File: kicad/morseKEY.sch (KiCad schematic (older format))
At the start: 11 parts

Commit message: schematic
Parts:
- removed P?: CONN_01X02, symbol CONN_01X02
- added P2: KEY, Pin_Headers:Pin_Header_Straight_1x03, symbol CONN_01X03
- added P3: ISP, Pin_Headers:Pin_Header_Straight_2x03, symbol CONN_02X03
- added R4: 2k2, Pin_Headers:Pin_Header_Straight_1x03, symbol R_VAR
- added R5: 2k2, Resistors_ThroughHole:Resistor_Horizontal_RM10mm, symbol R
- C1: renamed from C?; value C -> 100nF; footprint (none) -> Capacitors_ThroughHole:C_Disc_D3_P2.5
- C2: renamed from C?; value C -> 33uF,10V; footprint (none) -> Capacitors_ThroughHole:C_Radial_D5_L6_P2.5; symbol C -> C_POL; manf# (none) -> mfr_pn
- D1, D2: renamed from D?; value ZENERsmall -> 3V6; footprint (none) -> Diodes_ThroughHole:Diode_DO-35_SOD27_Horizontal_RM10
- P1: renamed from P?; footprint (none) -> Connect:USB_A
- R1: renamed from R?; value R -> 2k2; footprint (none) -> Resistors_ThroughHole:Resistor_Horizontal_RM10mm
- R2, R3: renamed from R?; value R -> 68E; footprint (none) -> Resistors_ThroughHole:Resistor_Horizontal_RM10mm
- SP1: renamed from SP?; value SPEAKER -> BUZ; footprint (none) -> Pin_Headers:Pin_Header_Straight_1x02
- U1: renamed from IC?; footprint DIP8 -> Housings_DIP:DIP-8_W7.62mm_LongPads
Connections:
- net labels added: 5V, D+, D-, GND, K1, K3, MISO, MOSI, RST, SCK
- wire segments 0 -> 59
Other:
- moved on the sheet: C1, C2, D1, D2, P1, R1, R2, R3

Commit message: board layout
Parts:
- C1: footprint Capacitors_ThroughHole:C_Disc_D3_P2.5 -> morseKEY:C_Disc_D3_P2.5
- C2: footprint Capacitors_ThroughHole:C_Radial_D5_L6_P2.5 -> morseKEY:C_Radial_D5_L6_P2.5
- D1, D2: footprint Diodes_ThroughHole:Diode_DO-35_SOD27_Horizontal_RM10 -> morseKEY:Diode_DO-41_SOD81_Vertical_KathodeUp
- P1: footprint Connect:USB_A -> morseKEY:USB_A
- P2: footprint Pin_Headers:Pin_Header_Straight_1x03 -> morseKEY:Pin_Header_Straight_1x03
- P3: footprint Pin_Headers:Pin_Header_Straight_2x03 -> morseKEY:Pin_Header_Straight_2x03
- R1, R2, R3: footprint Resistors_ThroughHole:Resistor_Horizontal_RM10mm -> morseKEY:Resistor_Vertical_RM5mm
- R4: value 2k2 -> 2k5; footprint Pin_Headers:Pin_Header_Straight_1x03 -> morseKEY:Pin_Header_Straight_1x03
- R5: value 2k2 -> 2k5; footprint Resistors_ThroughHole:Resistor_Horizontal_RM10mm -> morseKEY:Resistor_Vertical_RM5mm
- SP1: footprint Pin_Headers:Pin_Header_Straight_1x02 -> morseKEY:Pin_Header_Straight_1x04; symbol SPEAKER -> SPEAKER2; manf# (none) -> Value
- U1: footprint Housings_DIP:DIP-8_W7.62mm_LongPads -> morseKEY:DIP-8_W7.62mm_LongPads
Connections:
- wire segments 59 -> 62
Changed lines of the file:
@@
 F 0 "U1" H 4575 4200 50  0000 C CNB
 F 1 "ATTINY85-P" H 4750 4125 50  0000 C CNB
-F 2 "Housings_DIP:DIP-8_W7.62mm_LongPads" H 6725 3725 50  0000 C CIN
+F 2 "morseKEY:DIP-8_W7.62mm_LongPads" H 6725 3725 50  0001 C CIN
 F 3 "" H 5725 3725 50  0000 C CNN
 	1    5725 3725
@@
 F 0 "C1" H 7400 2975 50  0000 L CNB
 F 1 "100nF" H 7400 2775 50  0000 L CNN
-F 2 "Capacitors_ThroughHole:C_Disc_D3_P2.5" H 7413 2725 50  0001 C CNN
+F 2 "morseKEY:C_Disc_D3_P2.5" H 7413 2725 50  0001 C CNN
 F 3 "" H 7375 2875 50  0000 C CNN
 	1    7375 2875
@@
 F 0 "C2" H 7775 2975 50  0000 L CNB
 F 1 "33uF,10V" H 7775 2775 50  0000 L CNN
-F 2 "Capacitors_ThroughHole:C_Radial_D5_L6_P2.5" H 7788 2725 50  0001 C CNN
+F 2 "morseKEY:C_Radial_D5_L6_P2.5" H 7788 2725 50  0001 C CNN
 F 3 "" H 7750 2875 50  0000 C CNN
 F 4 "mfr_pn" H 7750 2875 60  0001 C CNN "manf#"
@@
 F 0 "R2" V 8150 3575 50  0000 C CNB
 F 1 "68E" V 8250 3575 50  0000 C CNN
-F 2 "Resistors_ThroughHole:Resistor_Horizontal_RM10mm" V 8180 3575 50  0001 C CNN
+F 2 "morseKEY:Resistor_Vertical_RM5mm" V 8180 3575 50  0001 C CNN
 F 3 "" H 8250 3575 50  0000 C CNN
 	1    8250 3575
@@
 F 0 "R3" V 8350 3675 50  0000 C CNB
 F 1 "68E" V 8250 3675 50  0000 C CNN
-F 2 "Resistors_ThroughHole:Resistor_Horizontal_RM10mm" V 8180 3675 50  0001 C CNN
+F 2 "morseKEY:Resistor_Vertical_RM5mm" V 8180 3675 50  0001 C CNN
 F 3 "" H 8250 3675 50  0000 C CNN
 	1    8250 3675
@@
 F 0 "R1" H 8825 2875 50  0000 C CNB
 F 1 "2k2" V 8925 2875 50  0000 C CNN
-F 2 "Resistors_ThroughHole:Resistor_Horizontal_RM10mm" V 8855 2875 50  0001 C CNN
+F 2 "morseKEY:Resistor_Vertical_RM5mm" V 8855 2875 50  0001 C CNN
 F 3 "" H 8925 2875 50  0000 C CNN
 	1    8925 2875
@@
 F 0 "D1" V 8725 4350 50  0000 C CNB
 F 1 "3V6" H 8775 4275 50  0000 C CNN
-F 2 "Diodes_ThroughHole:Diode_DO-35_SOD27_Horizontal_RM10" H 8625 4300 50  0001 C CNN
+F 2 "morseKEY:Diode_DO-41_SOD81_Vertical_KathodeUp" H 8625 4300 50  0001 C CNN
 F 3 "" H 8625 4300 50  0000 C CNN
 	1    8625 4300
@@
 F 0 "D2" V 9025 4350 50  0000 C CNB
 F 1 "3V6" H 9050 4275 50  0000 C CNN
-F 2 "Diodes_ThroughHole:Diode_DO-35_SOD27_Horizontal_RM10" H 8925 4300 50  0001 C CNN
+F 2 "morseKEY:Diode_DO-41_SOD81_Vertical_KathodeUp" H 8925 4300 50  0001 C CNN
 F 3 "" H 8925 4300 50  0000 C CNN
 	1    8925 4300
@@
 $EndComp
 $Comp
-L SPEAKER SP1
+L SPEAKER2 SP1
 U 1 1 5883265F
 P 2225 3250
 F 0 "SP1" H 2225 3575 50  0000 C CNB
 F 1 "BUZ" H 2225 3500 50  0000 C CNB
-F 2 "Pin_Headers:Pin_Header_Straight_1x02" H 2225 3250 50  0001 C CNN
+F 2 "morseKEY:Pin_Header_Straight_1x04" H 2225 3250 50  0001 C CNN
 F 3 "" H 2225 3250 50  0000 C CNN
+F 4 "Value" H 2225 3250 60  0001 C CNN "manf#"
 	1    2225 3250
 	-1   0    0    -1
@@
 F 0 "P1" V 9175 3675 50  0000 C CNB
 F 1 "USB_A" V 9250 3675 50  0000 C CNB
-F 2 "Connect:USB_A" V 9500 3575 50  0001 C CNN
+F 2 "morseKEY:USB_A" V 9500 3575 50  0001 C CNN
 F 3 "" V 9500 3575 50  0000 C CNN
 	1    9550 3675
@@
 F 0 "P2" H 2050 4250 50  0000 C CNB
 F 1 "KEY" H 2050 4175 50  0000 C CNB
-F 2 "Pin_Headers:Pin_Header_Straight_1x03" H 2050 3975 50  0001 C CNN
+F 2 "morseKEY:Pin_Header_Straight_1x03" H 2050 3975 50  0001 C CNN
 F 3 "" H 2050 3975 50  0000 C CNN
 	1    2050 3975
@@
 	2525 3350 2625 3350
 Wire Wire Line
-	2625 3350 2625 4850
+	2625 3300 2625 4850
 Wire Wire Line
 	2375 4850 9650 4850
@@
 P 3300 2875
 F 0 "R4" H 3200 2875 50  0000 C CNB
-F 1 "2k2" V 3300 2875 50  0000 C CNN
-F 2 "Pin_Headers:Pin_Header_Straight_1x03" V 3230 2875 50  0001 C CNN
+F 1 "2k5" V 3300 2875 50  0000 C CNN
+F 2 "morseKEY:Pin_Header_Straight_1x03" V 3230 2875 50  0001 C CNN
 F 3 "" H 3300 2875 50  0000 C CNN
 F 4 "mfr_pn" H 3300 2875 60  0001 C CNN "manf#"
@@
 P 3300 4325
 F 0 "R5" H 3200 4325 50  0000 C CNB
-F 1 "2k2" V 3300 4325 50  0000 C CNN
-F 2 "Resistors_ThroughHole:Resistor_Horizontal_RM10mm" V 3230 4325 50  0001 C CNN
+F 1 "2k5" V 3300 4325 50  0000 C CNN
+F 2 "morseKEY:Resistor_Vertical_RM5mm" V 3230 4325 50  0001 C CNN
 F 3 "" H 3300 4325 50  0000 C CNN
 	1    3300 4325
@@
 F 0 "P3" H 3225 6325 50  0000 C CNB
 F 1 "ISP" H 3225 5925 50  0000 C CNB
-F 2 "Pin_Headers:Pin_Header_Straight_2x03" H 3225 4925 50  0001 C CNN
+F 2 "morseKEY:Pin_Header_Straight_2x03" H 3225 4925 50  0001 C CNN
 F 3 "" H 3225 4925 50  0000 C CNN
 	1    3225 6125
@@
 Wire Wire Line
 	3975 6025 3975 5925
+Wire Wire Line
+	2525 3200 2625 3200
+Wire Wire Line
+	2625 3200 2625 3150
+Connection ~ 2625 3150
+Wire Wire Line
+	2525 3300 2625 3300
+Connection ~ 2625 3350
 $EndSCHEMATC

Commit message: 3D render
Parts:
- R4: footprint morseKEY:Pin_Header_Straight_1x03 -> morseKEY:res_vert
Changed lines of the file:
@@
 F 0 "R4" H 3200 2875 50  0000 C CNB
 F 1 "2k5" V 3300 2875 50  0000 C CNN
-F 2 "morseKEY:Pin_Header_Straight_1x03" V 3230 2875 50  0001 C CNN
+F 2 "morseKEY:res_vert" V 3230 2875 50  0001 C CNN
 F 3 "" H 3300 2875 50  0000 C CNN
 F 4 "mfr_pn" H 3300 2875 60  0001 C CNN "manf#"

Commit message: board layout
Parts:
- P1: footprint morseKEY:USB_A -> morseKEY:USB_A_up2-ah-th
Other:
- moved on the sheet: C1, C2, D1, D2, P1, P2, R1, R2, R3, R4, R5, SP1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

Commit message: gerbers
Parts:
- added G1: OSHW-LOGO, morseKEY:OSHW_logo_notext, symbol OSHW-LOGO
- added G2: CKT, morseKEY:morseKEY, symbol CONN_01X01
- added P4, P5: MTG, morseKEY:1pin, symbol CONN_01X01
- D1, D2: footprint morseKEY:Diode_DO-41_SOD81_Vertical_KathodeUp -> morseKEY:Diode_DO-41_SOD81_Vertical_KathodeUp_2
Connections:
- no-connect marks 0 -> 3
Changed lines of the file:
@@
 LIBS:contrib
 LIBS:valves
+LIBS:ultim8x64_sym
+LIBS:uControl
+LIBS:mmM
 LIBS:morseKEY-cache
 EELAYER 25 0
@@
 F 0 "D1" V 8250 4350 50  0000 C CNB
 F 1 "3V6" H 8275 4250 50  0000 C CNN
-F 2 "morseKEY:Diode_DO-41_SOD81_Vertical_KathodeUp" H 8150 4300 50  0001 C CNN
+F 2 "morseKEY:Diode_DO-41_SOD81_Vertical_KathodeUp_2" H 8150 4300 50  0001 C CNN
 F 3 "" H 8150 4300 50  0000 C CNN
 	1    8150 4300
@@
 F 0 "D2" V 8450 4350 50  0000 C CNB
 F 1 "3V6" H 8475 4250 50  0000 C CNN
-F 2 "morseKEY:Diode_DO-41_SOD81_Vertical_KathodeUp" H 8350 4300 50  0001 C CNN
+F 2 "morseKEY:Diode_DO-41_SOD81_Vertical_KathodeUp_2" H 8350 4300 50  0001 C CNN
 F 3 "" H 8350 4300 50  0000 C CNN
 	1    8350 4300
@@
 	-1   0    0    -1
 $EndComp
+$Comp
+L CONN_01X01 P4
+U 1 1 58909FCB
+P 5375 6050
+F 0 "P4" H 5375 6150 50  0000 C CNN
+F 1 "MTG" V 5475 6050 50  0000 C CNN
+F 2 "morseKEY:1pin" H 5375 6050 50  0001 C CNN
+F 3 "" H 5375 6050 50  0000 C CNN
+	1    5375 6050
+	0    -1   -1   0
+$EndComp
+$Comp
+L CONN_01X01 P5
+U 1 1 5890A054
+P 5775 6050
+F 0 "P5" H 5775 6150 50  0000 C CNN
+F 1 "MTG" V 5875 6050 50  0000 C CNN
+F 2 "morseKEY:1pin" H 5775 6050 50  0001 C CNN
+F 3 "" H 5775 6050 50  0000 C CNN
+	1    5775 6050
+	0    -1   -1   0
+$EndComp
+NoConn ~ 5375 6250
+NoConn ~ 5775 6250
+$Comp
+L OSHW-LOGO G1
+U 1 1 5890D05B
+P 10875 6800
+F 0 "G1" H 10875 6800 50  0001 C CNN
+F 1 "OSHW-LOGO" H 10875 6800 50  0001 C CNN
+F 2 "morseKEY:OSHW_logo_notext" H 10905 6950 20  0001 C CNN
+F 3 "" H 10875 6800 60  0000 C CNN
+F 4 "mfr_pn" H 10875 6800 60  0001 C CNN "manf#"
+	1    10875 6800
+	1    0    0    -1
+$EndComp
+$Comp
+L CONN_01X01 G2
+U 1 1 5890F12E
+P 5350 6600
+F 0 "G2" H 5350 6700 50  0000 C CNN
+F 1 "CKT" V 5450 6600 50  0000 C CNN
+F 2 "morseKEY:morseKEY" H 5350 6600 50  0001 C CNN
+F 3 "" H 5350 6600 50  0000 C CNN
+	1    5350 6600
+	0    -1   -1   0
+$EndComp
+NoConn ~ 5350 6800
 $EndSCHEMATC

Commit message: BoM
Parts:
- R4: value 2k5 -> 1k5
- R5: value 2k5 -> 3k3
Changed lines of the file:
@@
 LIBS:morseKEY
 LIBS:power
-LIBS:device
-LIBS:transistors
-LIBS:conn
-LIBS:linear
-LIBS:regul
-LIBS:74xx
-LIBS:cmos4000
-LIBS:adc-dac
-LIBS:memory
-LIBS:xilinx
-LIBS:microcontrollers
-LIBS:dsp
-LIBS:microchip
-LIBS:analog_switches
-LIBS:motorola
-LIBS:texas
-LIBS:intel
-LIBS:audio
-LIBS:interface
-LIBS:digital-audio
-LIBS:philips
-LIBS:display
-LIBS:cypress
-LIBS:siliconi
-LIBS:opto
-LIBS:atmel
-LIBS:contrib
-LIBS:valves
-LIBS:ultim8x64_sym
-LIBS:uControl
-LIBS:mmM
 LIBS:morseKEY-cache
 EELAYER 25 0
@@
 P 3825 3250
 F 0 "R4" H 3725 3250 50  0000 C CNB
-F 1 "2k5" V 3825 3250 50  0000 C CNN
+F 1 "1k5" V 3825 3250 50  0000 C CNN
 F 2 "morseKEY:res_vert" V 3755 3250 50  0001 C CNN
 F 3 "" H 3825 3250 50  0000 C CNN
@@
 P 3825 4325
 F 0 "R5" H 3725 4325 50  0000 C CNB
-F 1 "2k5" V 3825 4325 50  0000 C CNN
+F 1 "3k3" V 3825 4325 50  0000 C CNN
 F 2 "morseKEY:Resistor_Vertical_RM5mm" V 3755 4325 50  0001 C CNN
 F 3 "" H 3825 4325 50  0000 C CNN

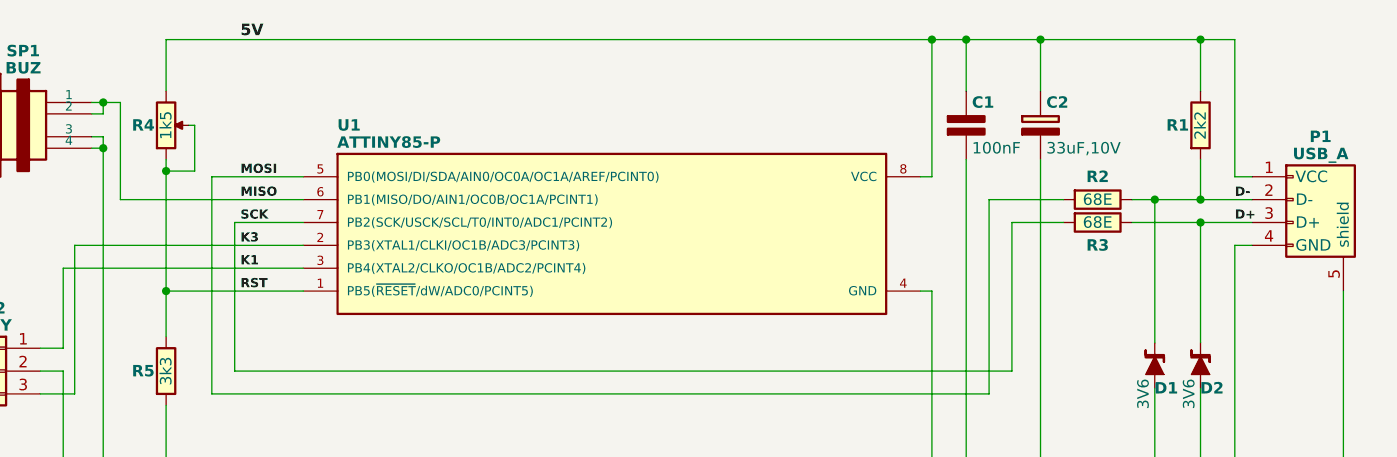
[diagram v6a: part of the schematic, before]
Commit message: changed RST resistor divider
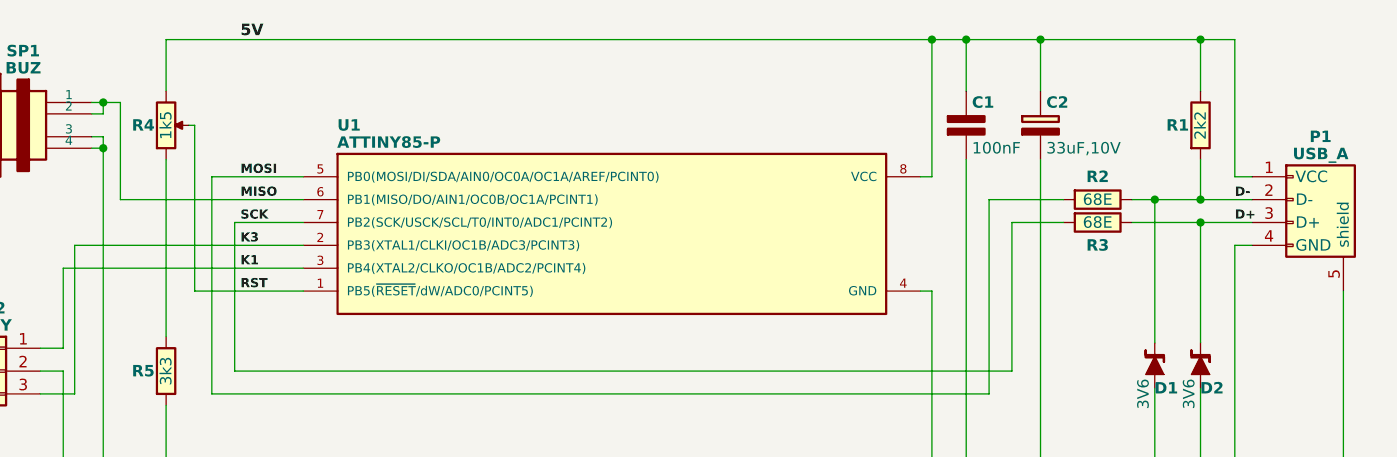
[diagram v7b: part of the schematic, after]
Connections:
- net RST: no longer R4.2, R5.1
- new net: R4.2, R5.1
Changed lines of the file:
@@
 	8575 3475 8500 3475
 Wire Wire Line
-	8500 3475 8500 2875
-Wire Wire Line
-	8500 2875 3825 2875
+	8500 2875 8500 3475
+Wire Wire Line
+	3825 2875 8500 2875
 Wire Wire Line
 	7175 2875 7175 3475
@@
 	3825 4475 3825 4850
 Connection ~ 3825 4850
-Wire Wire Line
-	4425 3975 3825 3975
-Connection ~ 3825 3975
-Wire Wire Line
-	3925 3250 3950 3250
-Wire Wire Line
-	3950 3250 3950 3450
-Wire Wire Line
-	3950 3450 3825 3450
-Connection ~ 3825 3450
 $Comp
 L CONN_02X03 P3
@@
 $EndComp
 NoConn ~ 5350 6800
+Wire Wire Line
+	3925 3250 3950 3250
+Wire Wire Line
+	3950 3250 3950 3975
+Wire Wire Line
+	3950 3975 4425 3975
 $EndSCHEMATC

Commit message: morseKEY update for KiCad FreeCAD demo tutorial
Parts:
- added P6: MTG, morseKEY:1pin, symbol morseKEY-rescue:CONN_01X01
- C1: symbol C -> morseKEY:C
- C2: symbol C_POL -> morseKEY:C_POL
- D1, D2: symbol ZENERsmall -> morseKEY:ZENERsmall
- G1: symbol OSHW-LOGO -> morseKEY:OSHW-LOGO
- G2, P4, P5: symbol CONN_01X01 -> morseKEY-rescue:CONN_01X01
- P1: symbol USB_A -> morseKEY:USB_A
- P2: symbol CONN_01X03 -> morseKEY:CONN_01X03
- P3: symbol CONN_02X03 -> morseKEY:CONN_02X03
- R1, R2, R3, R5: symbol R -> morseKEY:R
- R4: symbol R_VAR -> morseKEY:R_VAR
- SP1: symbol SPEAKER2 -> morseKEY:SPEAKER2
- U1: symbol ATTINY85-P -> morseKEY:ATTINY85-P
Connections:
- net RST: now also R4.2; no longer R4.3
- net at R5.1: now also R4.3; no longer R4.2
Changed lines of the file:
@@
-EESchema Schematic File Version 2
-LIBS:morseKEY
-LIBS:power
-LIBS:morseKEY-cache
-EELAYER 25 0
+EESchema Schematic File Version 4
+EELAYER 30 0
 EELAYER END
 $Descr A4 11693 8268
@@
 $EndDescr
 $Comp
-L ATTINY85-P U1
+L morseKEY:ATTINY85-P U1
 U 1 1 5883248B
 P 5775 3725
@@
 $EndComp
 $Comp
-L C C1
+L morseKEY:C C1
 U 1 1 58832568
 P 7325 3250
@@
 $EndComp
 $Comp
-L C_POL C2
+L morseKEY:C_POL C2
 U 1 1 5883258F
 P 7650 3250
@@
 $EndComp
 $Comp
-L R R2
+L morseKEY:R R2
 U 1 1 588325AA
 P 7900 3575
@@
 $EndComp
 $Comp
-L R R3
+L morseKEY:R R3
 U 1 1 588325C7
 P 7900 3675
@@
 $EndComp
 $Comp
-L R R1
+L morseKEY:R R1
 U 1 1 588325E6
 P 8350 3250
@@
 $EndComp
 $Comp
-L ZENERsmall D1
+L morseKEY:ZENERsmall D1
 U 1 1 58832607
 P 8150 4300
@@
 $EndComp
 $Comp
-L ZENERsmall D2
+L morseKEY:ZENERsmall D2
 U 1 1 5883263A
 P 8350 4300
@@
 $EndComp
 $Comp
-L SPEAKER2 SP1
+L morseKEY:SPEAKER2 SP1
 U 1 1 5883265F
 P 3200 3250
@@
 $EndComp
 $Comp
-L USB_A P1
+L morseKEY:USB_A P1
 U 1 1 588326BD
 P 8875 3675
@@
 	8500 2875 8500 3475
 Wire Wire Line
-	3825 2875 8500 2875
+	3825 2875 7175 2875
 Wire Wire Line
 	7175 2875 7175 3475
@@
 Connection ~ 8350 2875
 Wire Wire Line
-	8050 3575 8575 3575
-Wire Wire Line
-	8050 3675 8575 3675
+	8050 3575 8150 3575
+Wire Wire Line
+	8050 3675 8350 3675
 Wire Wire Line
 	8150 4200 8150 3575
@@
 Connection ~ 8350 3575
 Wire Wire Line
-	3500 3150 3625 3150
+	3500 3150 3550 3150
 Wire Wire Line
 	3625 3150 3625 3575
@@
 	3500 3350 3550 3350
 Wire Wire Line
-	3550 3300 3550 4850
-Wire Wire Line
-	3375 4850 8975 4850
+	3550 3300 3550 3350
+Wire Wire Line
+	3375 4850 3550 4850
 Wire Wire Line
 	8500 4850 8500 3775
@@
 	3425 3775 4425 3775
 $Comp
-L R_VAR R4
+L morseKEY:R_VAR R4
 U 1 1 588DF207
 P 3825 3250
@@
 $EndComp
 $Comp
-L R R5
+L morseKEY:R R5
 U 1 1 588DF479
 P 3825 4325
@@
 Connection ~ 3825 4850
 $Comp
-L CONN_02X03 P3
+L morseKEY:CONN_02X03 P3
 U 1 1 588E044D
 P 3225 6125
@@
 5V
 $Comp
-L PWR_FLAG #FLG01
+L power1:PWR_FLAG #FLG01
 U 1 1 588E17BF
 P 3975 5925
@@
 $EndComp
 $Comp
-L PWR_FLAG #FLG02
+L power1:PWR_FLAG #FLG02
 U 1 1 588E1825
 P 3975 6325
@@
 	3275 4325 3375 4325
 $Comp
-L CONN_01X03 P2
+L morseKEY:CONN_01X03 P2
 U 1 1 588DEE41
 P 3075 4325
@@
 $EndComp
 $Comp
-L CONN_01X01 P4
+L morseKEY-rescue:CONN_01X01 P4
 U 1 1 58909FCB
 P 5375 6050
@@
 $EndComp
 $Comp
-L CONN_01X01 P5
+L morseKEY-rescue:CONN_01X01 P5
 U 1 1 5890A054
 P 5775 6050
@@
 NoConn ~ 5775 6250
 $Comp
-L OSHW-LOGO G1
+L morseKEY:OSHW-LOGO G1
 U 1 1 5890D05B
 P 10875 6800
@@
 $EndComp
 $Comp
-L CONN_01X01 G2
+L morseKEY-rescue:CONN_01X01 G2
 U 1 1 5890F12E
 P 5350 6600
@@
 Wire Wire Line
 	3950 3975 4425 3975
+Wire Wire Line
+	7325 2875 7650 2875
+Wire Wire Line
+	7650 2875 8350 2875
+Wire Wire Line
+	8350 2875 8500 2875
+Wire Wire Line
+	8150 3575 8350 3575
+Wire Wire Line
+	8350 3675 8575 3675
+Wire Wire Line
+	8350 3575 8575 3575
+Wire Wire Line
+	8500 4850 8975 4850
+Wire Wire Line
+	8350 4850 8500 4850
+Wire Wire Line
+	8150 4850 8350 4850
+Wire Wire Line
+	7650 4850 8150 4850
+Wire Wire Line
+	7325 4850 7650 4850
+Wire Wire Line
+	7175 4850 7325 4850
+Wire Wire Line
+	3550 4850 3825 4850
+Wire Wire Line
+	7175 2875 7325 2875
+Wire Wire Line
+	3825 4850 7175 4850
+Wire Wire Line
+	3550 3150 3625 3150
+Wire Wire Line
+	3550 3350 3550 4850
+$Comp
+L morseKEY-rescue:CONN_01X01 P6
+U 1 1 5E9978EB
+P 6175 6050
+F 0 "P6" H 6175 6150 50  0000 C CNN
+F 1 "MTG" V 6275 6050 50  0000 C CNN
+F 2 "morseKEY:1pin" H 6175 6050 50  0001 C CNN
+F 3 "" H 6175 6050 50  0000 C CNN
+	1    6175 6050
+	0    -1   -1   0
+$EndComp
 $EndSCHEMATC
